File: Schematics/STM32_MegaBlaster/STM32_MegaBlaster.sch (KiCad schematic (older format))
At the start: 85 parts, among them J1 SD_Card, J2 USB_B, J3 Barrel_Jack, J4 AMP_OUT, SW1 PREV, SW2 RAND, SW3 NEXT, SW4 OPTION, SW5 PWR_SWITCH, SW6 MUTE_SN, U1 BluePill_STM32F103C, U10 LD1117S33, U11 LM2596T-5, U12 I2C_OLED, U2 SN769486, U3 YM2612, U4 CH340G, U5 LTC6904, U6 LTC6904, U7 23LC1024, U8 TL062, U9 TPA3122D2, Y1 12MHz

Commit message: Correct amplifier circuit and changed a couple footprints
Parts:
- added C38: 1uF, Capacitors_THT:C_Disc_D4.7mm_W2.5mm_P5.00mm, symbol device:C_Small
- C19, C31, C32: footprint Capacitors_THT:C_Disc_D3.0mm_W1.6mm_P2.50mm -> Capacitors_THT:C_Disc_D4.7mm_W2.5mm_P5.00mm
- C35: footprint Capacitors_THT:C_Disc_D3.0mm_W1.6mm_P2.50mm -> Capacitors_THT:CP_Radial_D6.3mm_P2.50mm
- D1: value SS34 -> SS34FACT-ND; footprint Diodes:DO-214AB -> Diodes_SMD:D_SOD-123F
- SW5: value PWR_SWITCH -> POWER
- SW6: value MUTE_SN -> MUTE PSG
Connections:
- wire segments 216 -> 215
- no-connect marks 22 -> 23
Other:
- moved on the sheet: C19, C36, D1, R6, SW6
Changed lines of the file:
@@
 P 4000 5800
 F 0 "SW5" V 3954 5898 50  0000 L CNN
-F 1 "PWR_SWITCH" V 4045 5898 50  0000 L CNN
+F 1 "POWER" V 4045 5898 50  0000 L CNN
 F 2 "Switches:1825115-1" H 4000 5800 50  0001 C CNN
 F 3 "" H 4000 5800 50  0001 C CNN
@@
 L device:D_Schottky_Small_ALT D1
 U 1 1 5AE5E4F2
-P 6200 6400
-F 0 "D1" V 6154 6468 50  0000 L CNN
-F 1 "SS34" V 6245 6468 50  0000 L CNN
-F 2 "Diodes:DO-214AB" V 6200 6400 50  0001 C CNN
-F 3 "" V 6200 6400 50  0001 C CNN
-	1    6200 6400
-	0    1    1    0
-$EndComp
-Wire Wire Line
-	6200 6300 6200 6200
+P 6200 6650
+F 0 "D1" V 6154 6718 50  0000 L CNN
+F 1 "SS34FACT-ND" V 6245 6718 50  0000 L CNN
+F 2 "Diodes_SMD:D_SOD-123F" V 6200 6650 50  0001 C CNN
+F 3 "" V 6200 6650 50  0001 C CNN
+	1    6200 6650
+	0    1    1    0
+$EndComp
 $Comp
 L power:GND #PWR0142
 U 1 1 5AE60EB9
-P 6200 6500
-F 0 "#PWR0142" H 6200 6250 50  0001 C CNN
-F 1 "GND" H 6205 6327 50  0000 C CNN
-F 2 "" H 6200 6500 50  0001 C CNN
-F 3 "" H 6200 6500 50  0001 C CNN
-	1    6200 6500
+P 6200 6750
+F 0 "#PWR0142" H 6200 6500 50  0001 C CNN
+F 1 "GND" H 6205 6577 50  0000 C CNN
+F 2 "" H 6200 6750 50  0001 C CNN
+F 3 "" H 6200 6750 50  0001 C CNN
+	1    6200 6750
 	1    0    0    -1
 $EndComp
@@
 Text GLabel 11300 6800 3    50   Input ~ 0
 AGND
-Text GLabel 11850 5850 0    50   Input ~ 0
+Text GLabel 11600 5850 0    50   Input ~ 0
 SN_OUT
 Text GLabel 12500 6300 0    50   Input ~ 0
@@
 L device:C_Small C19
 U 1 1 5AEC8A20
-P 12650 5850
-F 0 "C19" H 12400 5850 50  0000 L CNN
-F 1 "220pF" H 12400 5750 50  0000 L CNN
-F 2 "Capacitors_THT:C_Disc_D3.0mm_W1.6mm_P2.50mm" H 12650 5850 50  0001 C CNN
-F 3 "" H 12650 5850 50  0001 C CNN
-	1    12650 5850
+P 12400 5850
+F 0 "C19" H 12150 5850 50  0000 L CNN
+F 1 "220pF" H 12150 5750 50  0000 L CNN
+F 2 "Capacitors_THT:C_Disc_D4.7mm_W2.5mm_P5.00mm" H 12400 5850 50  0001 C CNN
+F 3 "" H 12400 5850 50  0001 C CNN
+	1    12400 5850
 	1    0    0    -1
 $EndComp
@@
 L power:GND #PWR0149
 U 1 1 5AEC9E79
-P 12650 5950
-F 0 "#PWR0149" H 12650 5700 50  0001 C CNN
-F 1 "GND" H 12655 5777 50  0000 C CNN
-F 2 "" H 12650 5950 50  0001 C CNN
-F 3 "" H 12650 5950 50  0001 C CNN
-	1    12650 5950
+P 12400 5950
+F 0 "#PWR0149" H 12400 5700 50  0001 C CNN
+F 1 "GND" H 12405 5777 50  0000 C CNN
+F 2 "" H 12400 5950 50  0001 C CNN
+F 3 "" H 12400 5950 50  0001 C CNN
+	1    12400 5950
 	1    0    0    -1
 $EndComp
@@
 L device:R R6
 U 1 1 5AECA1BB
-P 12800 5900
-F 0 "R6" H 12870 5946 50  0000 L CNN
-F 1 "2.2k" V 12800 5800 50  0000 L CNN
-F 2 "Resistors_THT:R_Axial_DIN0207_L6.3mm_D2.5mm_P7.62mm_Horizontal" V 12730 5900 50  0001 C CNN
-F 3 "" H 12800 5900 50  0001 C CNN
-	1    12800 5900
-	1    0    0    -1
-$EndComp
-Wire Wire Line
-	12650 5750 12800 5750
-Connection ~ 12650 5750
+P 12550 5900
+F 0 "R6" H 12620 5946 50  0000 L CNN
+F 1 "2.2k" V 12550 5800 50  0000 L CNN
+F 2 "Resistors_THT:R_Axial_DIN0207_L6.3mm_D2.5mm_P7.62mm_Horizontal" V 12480 5900 50  0001 C CNN
+F 3 "" H 12550 5900 50  0001 C CNN
+	1    12550 5900
+	1    0    0    -1
+$EndComp
+Wire Wire Line
+	12400 5750 12550 5750
+Connection ~ 12400 5750
 $Comp
 L power:GND #PWR0150
 U 1 1 5AECEC09
-P 12800 6050
-F 0 "#PWR0150" H 12800 5800 50  0001 C CNN
-F 1 "GND" H 12805 5877 50  0000 C CNN
-F 2 "" H 12800 6050 50  0001 C CNN
-F 3 "" H 12800 6050 50  0001 C CNN
-	1    12800 6050
-	1    0    0    -1
-$EndComp
-Connection ~ 12800 5750
+P 12550 6050
+F 0 "#PWR0150" H 12550 5800 50  0001 C CNN
+F 1 "GND" H 12555 5877 50  0000 C CNN
+F 2 "" H 12550 6050 50  0001 C CNN
+F 3 "" H 12550 6050 50  0001 C CNN
+	1    12550 6050
+	1    0    0    -1
+$EndComp
+Connection ~ 12550 5750
 Wire Wire Line
 	12500 6300 12600 6300
@@
 Wire Wire Line
 	13150 5750 13150 5900
-Wire Wire Line
-	12800 5750 13150 5750
 $Comp
 L device:R R9
@@
 	0    1    1    0
 $EndComp
-Connection ~ 13150 5750
 $Comp
 L device:R R10
@@
 L switches:SW_Push_SPDT SW6
 U 1 1 5AF99B60
-P 12150 5750
-F 0 "SW6" H 12150 5500 50  0000 C CNN
-F 1 "MUTE_SN" H 12150 5600 50  0000 C CNN
-F 2 "Switches:1825115-1" H 12150 5750 50  0001 C CNN
-F 3 "" H 12150 5750 50  0001 C CNN
-	1    12150 5750
+P 11900 5750
+F 0 "SW6" H 11900 5500 50  0000 C CNN
+F 1 "MUTE PSG" H 11900 5600 50  0000 C CNN
+F 2 "Switches:1825115-1" H 11900 5750 50  0001 C CNN
+F 3 "" H 11900 5750 50  0001 C CNN
+	1    11900 5750
 	-1   0    0    1
 $EndComp
 Wire Wire Line
-	11850 5850 11950 5850
-Wire Wire Line
-	12350 5750 12650 5750
+	11600 5850 11700 5850
+Wire Wire Line
+	12100 5750 12400 5750
 $Comp
 L power:+12V #PWR04
@@
 	10250 2250 10300 2250
 Connection ~ 10250 2150
-$Comp
-L power:GND #PWR01
-U 1 1 5AFD80DD
-P 11950 5650
-F 0 "#PWR01" H 11950 5400 50  0001 C CNN
-F 1 "GND" V 11955 5522 50  0000 R CNN
-F 2 "" H 11950 5650 50  0001 C CNN
-F 3 "" H 11950 5650 50  0001 C CNN
-	1    11950 5650
-	0    1    1    0
-$EndComp
 Wire Wire Line
 	10000 2250 10150 2250
@@
 F 0 "C31" V 12250 2250 50  0000 C CNN
 F 1 "0.22uF" V 12400 2350 50  0000 C CNN
-F 2 "Capacitors_THT:C_Disc_D3.0mm_W1.6mm_P2.50mm" H 12300 2350 50  0001 C CNN
+F 2 "Capacitors_THT:C_Disc_D4.7mm_W2.5mm_P5.00mm" H 12300 2350 50  0001 C CNN
 F 3 "" H 12300 2350 50  0001 C CNN
 	1    12300 2350
@@
 $EndComp
 $Comp
-L device:L_Small L5
-U 1 1 5B1B9873
-P 12550 2950
-F 0 "L5" V 12600 2950 50  0000 C CNN
-F 1 "22uH" V 12500 2950 50  0000 C CNN
-F 2 "Inductors_THT:L_Radial_D8.7mm_P5.00mm_Fastron_07HCP" H 12550 2950 50  0001 C CNN
-F 3 "" H 12550 2950 50  0001 C CNN
-	1    12550 2950
-	0    -1   -1   0
-$EndComp
-Wire Wire Line
-	12000 2950 12450 2950
-$Comp
-L device:C_Small C32
-U 1 1 5B1C754F
-P 12300 2850
-F 0 "C32" V 12350 2750 50  0000 C CNN
-F 1 "0.22uF" V 12200 2850 50  0000 C CNN
-F 2 "Capacitors_THT:C_Disc_D3.0mm_W1.6mm_P2.50mm" H 12300 2850 50  0001 C CNN
-F 3 "" H 12300 2850 50  0001 C CNN
-	1    12300 2850
-	0    1    1    0
-$EndComp
-Wire Wire Line
-	12400 2850 12450 2850
-Wire Wire Line
-	12450 2850 12450 2950
-Connection ~ 12450 2950
-Wire Wire Line
-	12200 2850 12000 2850
-Wire Wire Line
-	12000 3050 12450 3050
-Wire Wire Line
-	12450 3050 12450 3150
-Wire Wire Line
-	12450 3150 12750 3150
-$Comp
-L device:C_Small C35
-U 1 1 5B1E70F9
-P 12750 3050
-F 0 "C35" H 12842 3096 50  0000 L CNN
-F 1 "68nF" H 12842 3005 50  0000 L CNN
-F 2 "Capacitors_THT:C_Disc_D3.0mm_W1.6mm_P2.50mm" H 12750 3050 50  0001 C CNN
-F 3 "" H 12750 3050 50  0001 C CNN
-	1    12750 3050
-	1    0    0    -1
-$EndComp
-Connection ~ 12750 3150
-Wire Wire Line
-	12650 2950 12750 2950
-Wire Wire Line
-	12750 2950 13200 2950
-Connection ~ 12750 2950
-$Comp
-L power:GND #PWR010
-U 1 1 5B204A37
-P 13200 2950
-F 0 "#PWR010" H 13200 2700 50  0001 C CNN
-F 1 "GND" H 13200 2800 50  0000 C CNN
-F 2 "" H 13200 2950 50  0001 C CNN
-F 3 "" H 13200 2950 50  0001 C CNN
-	1    13200 2950
-	1    0    0    -1
-$EndComp
-Wire Wire Line
-	12750 3150 13400 3150
-$Comp
 L device:CP1_Small C36
 U 1 1 5B210924
-P 13500 3150
-F 0 "C36" V 13728 3150 50  0000 C CNN
-F 1 "1000uF" V 13637 3150 50  0000 C CNN
-F 2 "Capacitors_THT:CP_Radial_D8.0mm_P2.50mm" H 13500 3150 50  0001 C CNN
-F 3 "" H 13500 3150 50  0001 C CNN
-	1    13500 3150
-	0    -1   -1   0
-$EndComp
-Text GLabel 13600 3150 2    50   Input ~ 0
+P 13500 2950
+F 0 "C36" V 13728 2950 50  0000 C CNN
+F 1 "1000uF" V 13637 2950 50  0000 C CNN
+F 2 "Capacitors_THT:CP_Radial_D8.0mm_P2.50mm" H 13500 2950 50  0001 C CNN
+F 3 "" H 13500 2950 50  0001 C CNN
+	1    13500 2950
+	0    -1   -1   0
+$EndComp
+Text GLabel 13600 2950 2    50   Input ~ 0
 R_OUT
 $Comp
@@
 Wire Wire Line
 	2700 2950 3100 2950
+$Comp
+L device:C_Small C32
+U 1 1 5AF06548
+P 12300 2850
+F 0 "C32" V 12071 2850 50  0000 C CNN
+F 1 "0.22uF" V 12162 2850 50  0000 C CNN
+F 2 "Capacitors_THT:C_Disc_D4.7mm_W2.5mm_P5.00mm" H 12300 2850 50  0001 C CNN
+F 3 "" H 12300 2850 50  0001 C CNN
+	1    12300 2850
+	0    1    1    0
+$EndComp
+Wire Wire Line
+	12200 2850 12000 2850
+$Comp
+L device:L_Small L5
+U 1 1 5AF1BD90
+P 12600 2950
+F 0 "L5" V 12785 2950 50  0000 C CNN
+F 1 "22uH" V 12694 2950 50  0000 C CNN
+F 2 "Inductors_THT:L_Radial_D8.7mm_P5.00mm_Fastron_07HCP" H 12600 2950 50  0001 C CNN
+F 3 "" H 12600 2950 50  0001 C CNN
+	1    12600 2950
+	0    -1   -1   0
+$EndComp
+Wire Wire Line
+	12000 2950 12400 2950
+Wire Wire Line
+	12400 2850 12400 2950
+Connection ~ 12400 2950
+Wire Wire Line
+	12400 2950 12500 2950
+$Comp
+L device:C_Small C35
+U 1 1 5AF31A51
+P 12800 3050
+F 0 "C35" H 12892 3096 50  0000 L CNN
+F 1 "68nF" H 12892 3005 50  0000 L CNN
+F 2 "Capacitors_THT:CP_Radial_D6.3mm_P2.50mm" H 12800 3050 50  0001 C CNN
+F 3 "" H 12800 3050 50  0001 C CNN
+	1    12800 3050
+	1    0    0    -1
+$EndComp
+Wire Wire Line
+	12700 2950 12800 2950
+Wire Wire Line
+	12800 2950 13400 2950
+Connection ~ 12800 2950
+Wire Wire Line
+	12000 3050 12600 3050
+Wire Wire Line
+	12600 3050 12600 3150
+Wire Wire Line
+	12600 3150 12800 3150
+$Comp
+L power:GND #PWR01
+U 1 1 5AF754BD
+P 12800 3150
+F 0 "#PWR01" H 12800 2900 50  0001 C CNN
+F 1 "GND" H 12805 2977 50  0000 C CNN
+F 2 "" H 12800 3150 50  0001 C CNN
+F 3 "" H 12800 3150 50  0001 C CNN
+	1    12800 3150
+	1    0    0    -1
+$EndComp
+Connection ~ 12800 3150
+$Comp
+L device:C_Small C38
+U 1 1 5AF86E1C
+P 13050 5750
+F 0 "C38" V 12821 5750 50  0000 C CNN
+F 1 "1uF" V 12912 5750 50  0000 C CNN
+F 2 "Capacitors_THT:C_Disc_D4.7mm_W2.5mm_P5.00mm" H 13050 5750 50  0001 C CNN
+F 3 "" H 13050 5750 50  0001 C CNN
+	1    13050 5750
+	0    1    1    0
+$EndComp
+Connection ~ 13150 5750
+Wire Wire Line
+	12550 5750 12950 5750
+NoConn ~ 11700 5650
+Wire Wire Line
+	6200 6200 6200 6550
 $EndSCHEMATC

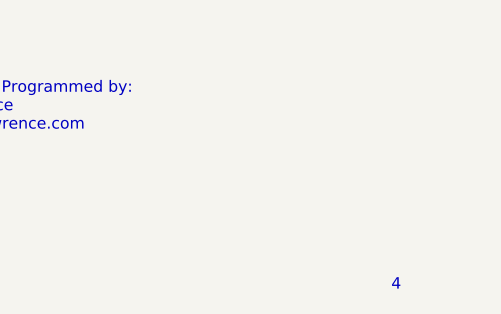
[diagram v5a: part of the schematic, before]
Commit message: Changed diode to more friendly package, moved OLED I2C lines far away from mixer circuit
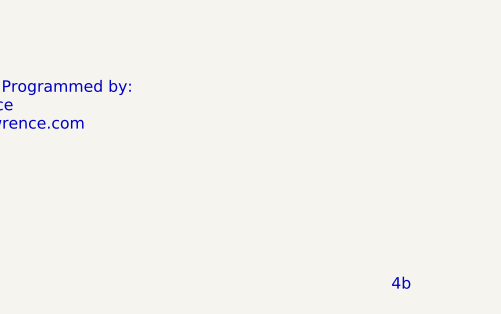
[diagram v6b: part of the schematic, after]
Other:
- note added: "4b"
- note removed: "4"
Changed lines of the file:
@@
 Connection ~ 9900 2750
 Text Notes 15550 11050 0    50   ~ 0
-4
+4b
 $Comp
 L power:+12V #PWR07

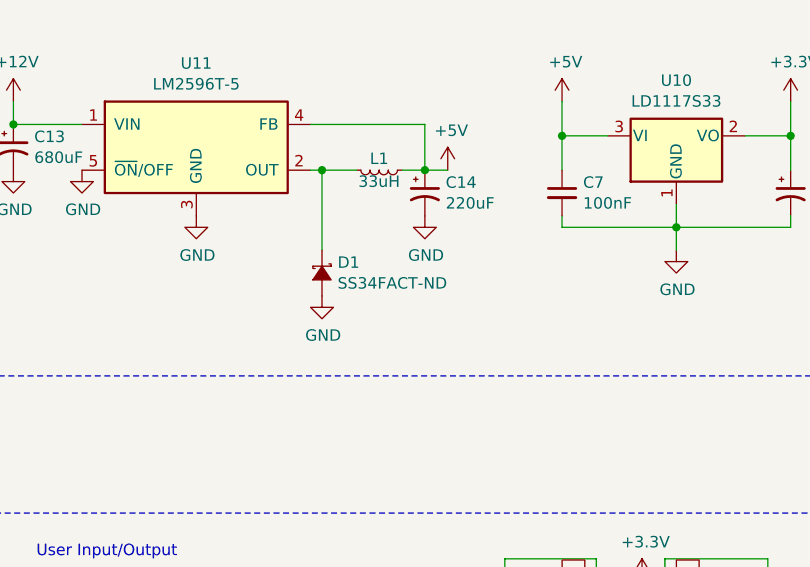
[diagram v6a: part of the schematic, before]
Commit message: Added better BOM
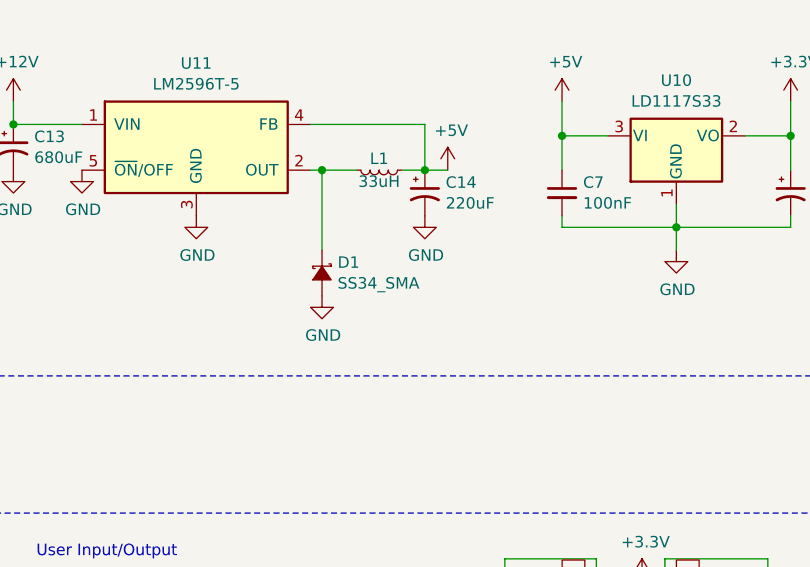
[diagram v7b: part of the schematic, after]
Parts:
- D1: value SS34FACT-ND -> SS34_SMA
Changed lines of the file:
@@
 P 6200 6650
 F 0 "D1" V 6154 6718 50  0000 L CNN
-F 1 "SS34FACT-ND" V 6245 6718 50  0000 L CNN
+F 1 "SS34_SMA" V 6245 6718 50  0000 L CNN
 F 2 "Diodes_SMD:D_SOD-123F" V 6200 6650 50  0001 C CNN
 F 3 "" V 6200 6650 50  0001 C CNN

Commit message: Corrected L4, L5 Inductor. 22uH to 2.2mH
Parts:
- L4, L5: value 22uH -> 2.2mH
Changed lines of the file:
@@
 P 12550 2250
 F 0 "L4" V 12600 2250 50  0000 C CNN
-F 1 "22uH" V 12500 2200 50  0000 C CNN
+F 1 "2.2mH" V 12500 2200 50  0000 C CNN
 F 2 "Inductors_THT:L_Radial_D8.7mm_P5.00mm_Fastron_07HCP" H 12550 2250 50  0001 C CNN
 F 3 "" H 12550 2250 50  0001 C CNN
@@
 P 12600 2950
 F 0 "L5" V 12785 2950 50  0000 C CNN
-F 1 "22uH" V 12694 2950 50  0000 C CNN
+F 1 "2.2mH" V 12694 2950 50  0000 C CNN
 F 2 "Inductors_THT:L_Radial_D8.7mm_P5.00mm_Fastron_07HCP" H 12600 2950 50  0001 C CNN
 F 3 "" H 12600 2950 50  0001 C CNN
